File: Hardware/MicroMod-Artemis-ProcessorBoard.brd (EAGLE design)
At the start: 22 x 22 mm, 40 parts, among them J1 MICROMOD-2222, U1 ARTEMIS_MODULESMD, U2 TSV524, U6 CH340E_MSOP10, Y1 32.768kHz

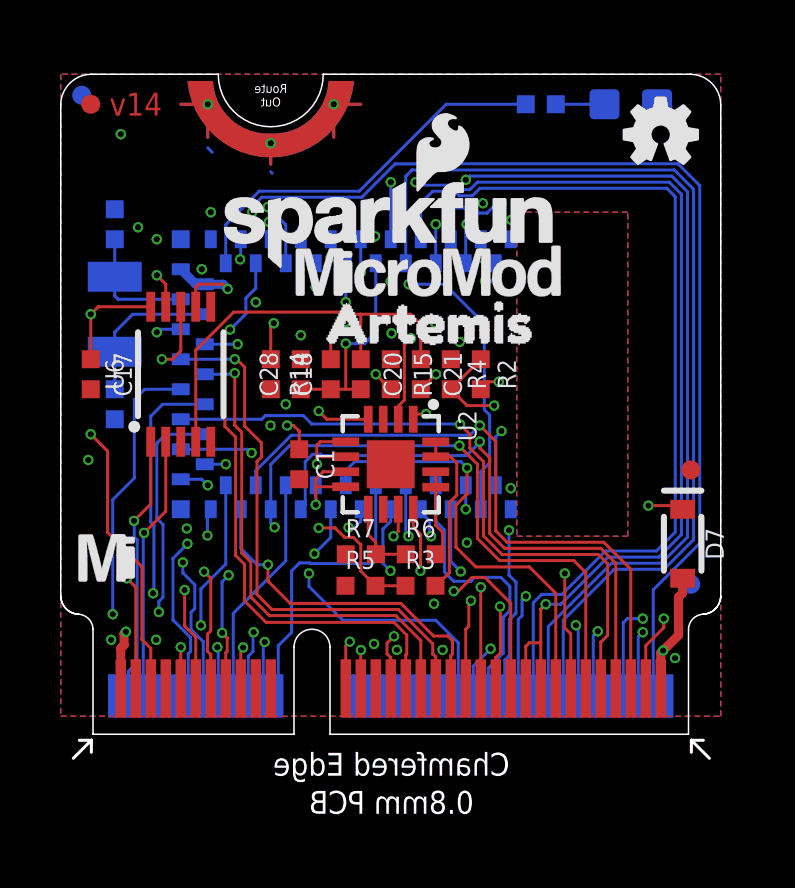
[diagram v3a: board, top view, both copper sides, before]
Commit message: Connect SPI pins to support Quad SPI. Move TX1 to AD12
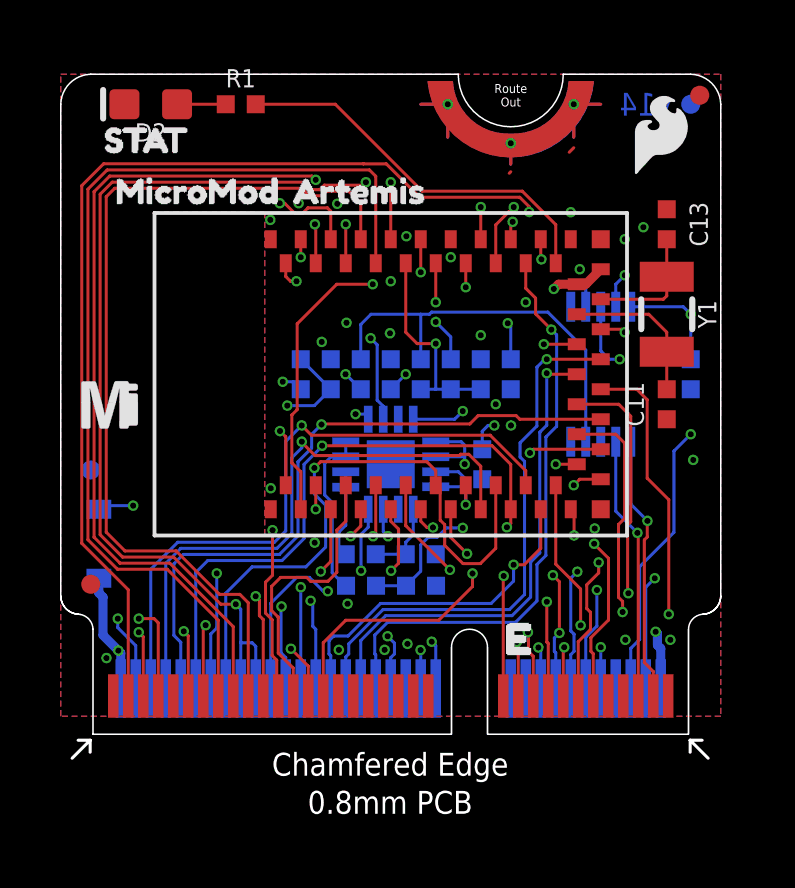
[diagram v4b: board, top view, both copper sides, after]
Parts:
- moved FRAME1 39.8 mm to (-8.89, -8.89), flipped to the top
- moved LOGO4 27.1 mm to (24.5, 50.8), flipped to the top
- moved FD2 20.6 mm to (21.3, 21.3), flipped to the top
- moved U$4 20.6 mm to (0.70, 19.8), flipped to the top
- moved C17 20.0 mm to (21.0, 12.0), flipped to the bottom
- moved FD1 20.0 mm to (1.00, 5.00), flipped to the top
- moved FD3 20.0 mm to (21.0, 21.0), flipped to the bottom
- moved FD4 20.0 mm to (1.00, 8.81), flipped to the bottom
- moved U$3 19.8 mm to (1.10, 18.1), flipped to the top
- moved D7 19.5 mm to (1.27, 6.35), flipped to the bottom
- moved U$7 19.0 mm to (20.5, 5.90), flipped to the bottom
- moved U$1 18.8 mm to (1.60, 11.0), flipped to the top
- moved C11 18.4 mm to (20.2, 11.0), flipped to the top
- moved C13 18.4 mm to (20.2, 17.0), flipped to the top
- moved Y1 18.4 mm to (20.2, 14.0), flipped to the top
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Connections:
- net SDIO_DATA1 renamed QSPI1
- net SDIO_DATA2 renamed QSPI2
- net SPI_!CS! renamed SPI_!CS!/QSPI3
- net SPI_MISO renamed SPI_MISO/QSPI0
- net SPI_MOSI renamed SPI_MOSI/QSPI_!CS!
- removed net ADC_D-: J1.65, U1.~AD12
- removed net SPI_SCK: J1.60, U1.~D5
- removed net TX1: J1.17, U1.~D24
- new net SPI_SCK/QSPI_CLK: J1.60, U1.~D24, U1.~D5
- new net TX1/ADC_D-: J1.17, J1.65, U1.~AD12
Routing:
- net TX1/ADC_D-: track 0.00 -> 28.3 mm, vias 0 -> 3
- net ADC_D-: track 25.2 -> 0.00 mm, vias 2 -> 0
- net SPI_SCK/QSPI_CLK: track 0.00 -> 21.1 mm, vias 0 -> 1
- net SPI_SCK: track 14.7 -> 0.00 mm, vias 1 -> 0
- net TX1: track 7.75 -> 0.00 mm
- net SWDIO: track 9.82 -> 9.49 mm, vias 0 -> 2
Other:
- outline, holes or cut-outs redrawn

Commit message: Adding additional decoupling, change version to v16.
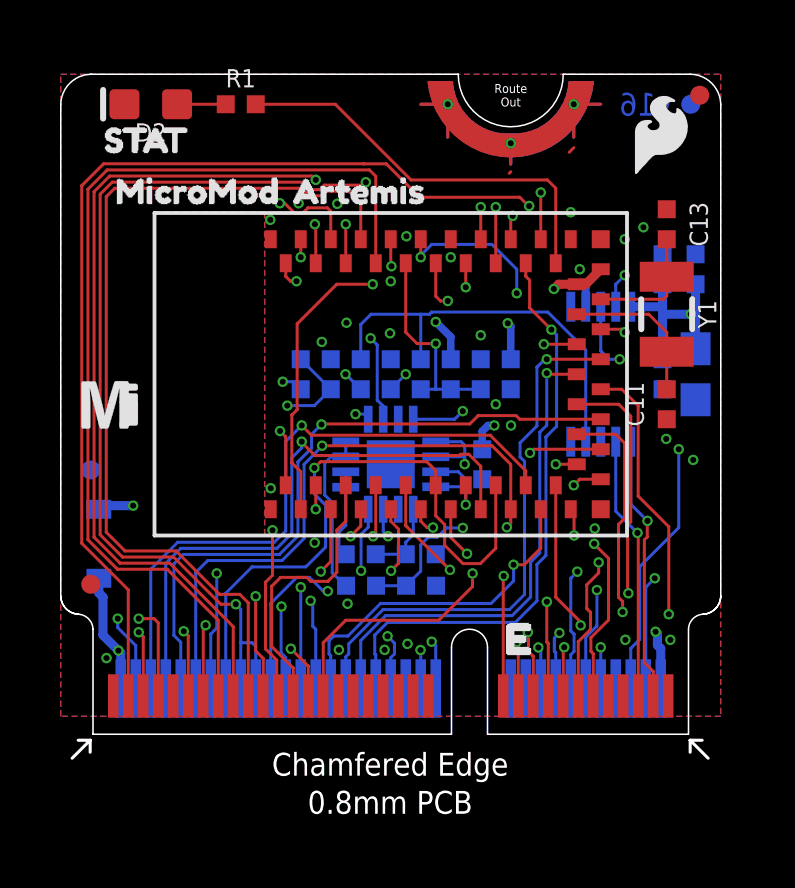
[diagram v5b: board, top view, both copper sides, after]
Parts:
- added C2: 0.22uF, SparkFun-Capacitors:0402-TIGHT
- added C3: 1.0uF, SparkFun-Capacitors:0402-TIGHT
- added C4: 10uF, SparkFun-Capacitors:0603
- R15: value 220KOHM-0402T-1/16W-1% -> 220K
- moved C17 3.62 mm to (20.1, 15.5), turned to 90 degrees
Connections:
- net SPI_SCK/QSPI_CLK renamed SPI_SCK/QSPI_SCK
- removed net CLKOUT: J1.56, J1.58, U1.D0
- new net CAM_MCLK: J1.56, J1.58, U1.~D18
- net 3.3V: now also C2.1, C3.1, C4.1
- net D0: now also U1.D0; no longer U1.D1
- net D1: now also U1.D1; no longer U1.D2
- net GND: now also C2.2, C3.2, C4.2
- net I2C_!INT!: now also U1.D2; no longer U1.~D18
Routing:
- net CAM_MCLK: track 0.00 -> 38.4 mm, vias 0 -> 3
- net CLKOUT: track 33.6 -> 0.00 mm, vias 3 -> 0
- net I2C_!INT!: track 15.5 -> 18.8 mm, vias 3 -> 2
- net 3.3V: track 17.7 -> 20.9 mm
- net GPIO5: track 41.7 -> 40.2 mm
- net D1: track 17.5 -> 18.8 mm
- net SCALED_BATT_VIN/3: track 19.8 -> 19.0 mm
- net D0: track 20.9 -> 21.7 mm
- net LED_BUILTIN: track 12.9 -> 13.7 mm
- net !RESET!: track 26.0 -> 25.5 mm
- net GND: vias 20 -> 21
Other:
- board text added: "v16"
- board text removed: "v14"

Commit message: Update SPI port 0/1 net names.
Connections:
- net SPI_!CS!/QSPI3 renamed SPI_!CS1!/QSPI3
- net SPI_!CS!1 renamed SPI_!CS!
- net SPI_MISO/QSPI0 renamed SPI_CIPO1/QSPI0
- net SPI_MISO1 renamed SPI_CIPO
- net SPI_MOSI/QSPI_!CS! renamed SPI_COPI1/QSPI_!CS!
- net SPI_MOSI1 renamed SPI_COPI
- net SPI_SCK/QSPI_SCK renamed SPI_SCK1/QSPI_SCK
- net SPI_SCK1 renamed SPI_SCK
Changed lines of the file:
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@@
 <elements>
 <element name="U1" library="SparkFun-IC-Microcontroller" package="ARTEMIS_FP" value="ARTEMIS_MODULESMD" x="11.5" y="12" smashed="yes" rot="R180">
-<attribute name="PROD_ID" value="SUB-14479" x="11.5" y="12" size="1.778" layer="27" font="vector" ratio="15" rot="R180" display="off"/>
+<attribute name="PROD_ID" value="SUB-14402" x="11.5" y="12" size="1.778" layer="27" font="vector" ratio="15" rot="R180" display="off"/>
 </element>
 <element name="FRAME1" library="SparkFun-Aesthetics" package="CREATIVE_COMMONS" value="FRAME-LEDGER" x="-8.89" y="-8.89" smashed="yes">
@@
 <wire x1="13.9352875" y1="11.1" x2="8.3009875" y2="11.1" width="0.1016" layer="2"/>
 </signal>
-<signal name="SPI_SCK1">
+<signal name="SPI_SCK">
 <contactref element="U1" pad="~D42"/>
 <wire x1="3.84568125" y1="6.1096" x2="2.143075" y2="6.1096" width="0.1016" layer="1"/>
@@
 <wire x1="5.292725" y1="4.66255625" x2="3.84568125" y2="6.1096" width="0.1016" layer="1"/>
 </signal>
-<signal name="SPI_MOSI1">
+<signal name="SPI_COPI">
 <contactref element="U1" pad="D38"/>
 <wire x1="5.75" y1="3.58736875" x2="3.63416875" y2="5.7032" width="0.1016" layer="1"/>
@@
 <wire x1="5.75" y1="1.275" x2="5.75" y2="3.58736875" width="0.1016" layer="1"/>
 </signal>
-<signal name="SPI_SCK/QSPI_SCK">
+<signal name="SPI_SCK1/QSPI_SCK">
 <contactref element="U1" pad="~D24"/>
 <contactref element="U1" pad="~D5"/>
@@
 <wire x1="8" y1="9.254875" x2="8.3626125" y2="9.6174875" width="0.1016" layer="15"/>
 </signal>
-<signal name="SPI_MISO/QSPI0">
+<signal name="SPI_CIPO1/QSPI0">
 <contactref element="U1" pad="~D22"/>
 <wire x1="15" y1="8.99391875" x2="15" y2="7.5" width="0.1016" layer="1"/>
@@
 <wire x1="8.1096" y1="6.52485" x2="8.1096" y2="8.99749375" width="0.1016" layer="16"/>
 </signal>
-<signal name="SPI_MOSI/QSPI_!CS!">
+<signal name="SPI_COPI1/QSPI_!CS!">
 <contactref element="U1" pad="D7"/>
 <wire x1="13" y1="7.5" x2="13" y2="6.5602" width="0.1016" layer="1"/>
@@
 <wire x1="5" y1="1.525" x2="5" y2="3.3416875" width="0.1016" layer="16"/>
 </signal>
-<signal name="SPI_!CS!/QSPI3">
+<signal name="SPI_!CS1!/QSPI3">
 <contactref element="U1" pad="~D23"/>
 <wire x1="3" y1="5.5" x2="3.9" y2="6.4" width="0.1016" layer="16"/>
@@
 <wire x1="17.41543125" y1="4.7446" x2="10.44478125" y2="4.7446" width="0.1016" layer="2"/>
 </signal>
-<signal name="SPI_MISO1">
+<signal name="SPI_CIPO">
 <contactref element="U1" pad="~D43"/>
 <wire x1="5.25" y1="3.8" x2="3.55" y2="5.5" width="0.1016" layer="1"/>
@@
 <wire x1="19.75" y1="1.275" x2="19.75" y2="2.094" width="0.1016" layer="1"/>
 </signal>
-<signal name="SPI_!CS!1">
+<signal name="SPI_!CS!">
 <contactref element="U1" pad="D41"/>
 <wire x1="14" y1="16.5" x2="14" y2="17.5714" width="0.1016" layer="1"/>

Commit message: Change 3.3V back feed diode to lower v-drop.
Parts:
- D7: value 1A/23V/620mV -> 3A/10V/280mV
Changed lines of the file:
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@@
 <?xml version="1.0" encoding="utf-8"?>
 <!DOCTYPE eagle SYSTEM "eagle.dtd">
-<eagle version="9.6.0">
+<eagle version="9.6.2">
 <drawing>
 <settings>
@@
 </element>
 <element name="LOGO1" library="SparkFun-Aesthetics" package="SFE_LOGO_NAME_FLAME_.1" value="SFE_LOGO_NAME_FLAME.1_INCH" x="11" y="17" smashed="yes" rot="MR0"/>
-<element name="D7" library="SparkFun-DiscreteSemi" package="SOD-323" value="1A/23V/620mV" x="1.27" y="6.35" smashed="yes" rot="MR270">
+<element name="D7" library="SparkFun-DiscreteSemi" package="SOD-323" value="3A/10V/280mV" x="1.27" y="6.35" smashed="yes" rot="MR270">
 <attribute name="NAME" x="0.508" y="6.35" size="0.6096" layer="26" font="vector" ratio="20" rot="MR270" align="bottom-center"/>
-<attribute name="PROD_ID" value="DIO-11623" x="1.27" y="7.62" size="1.778" layer="28" font="vector" ratio="15" rot="MR270" display="off"/>
-<attribute name="VALUE" x="2.032" y="6.35" size="0.6096" layer="28" font="vector" ratio="20" rot="MR270" align="top-center"/>
+<attribute name="PROD_ID" value="DIO-14072" x="1.27" y="7.62" size="1.778" layer="28" font="vector" ratio="15" rot="MR270" display="off"/>
+<attribute name="VALUE" value="3A/10V/280mV" x="2.032" y="6.35" size="0.6096" layer="28" font="vector" ratio="20" rot="MR270" align="top-center"/>
 </element>
 <element name="LOGO2" library="SparkFun-Aesthetics" package="SFE_LOGO_FLAME_.1" value="SFE_LOGO_FLAME.1_INCH" x="20" y="20" smashed="yes"/>

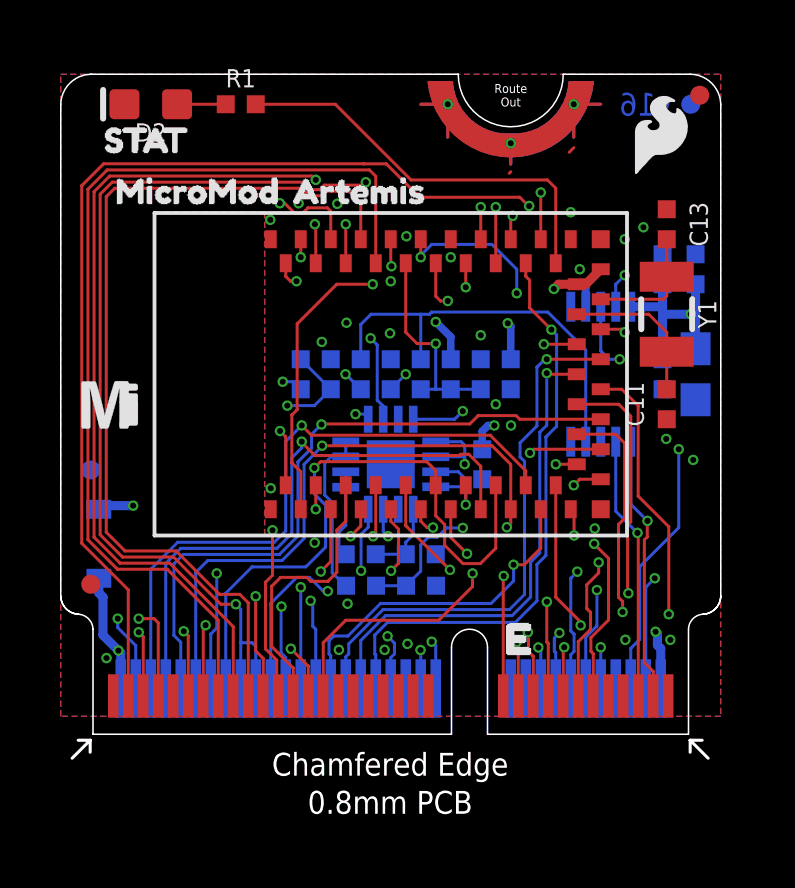
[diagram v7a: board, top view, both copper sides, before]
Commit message: Move CH340 to 3.3V side of diode. Replace D7 with 0.3uA leakage diode.
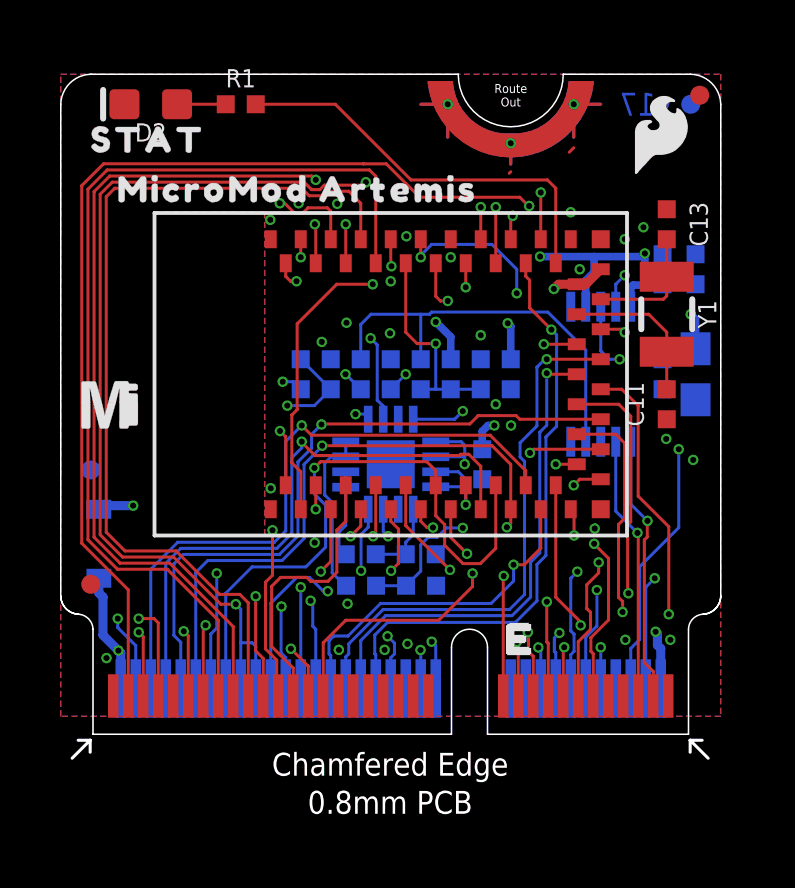
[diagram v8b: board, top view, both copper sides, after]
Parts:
- removed U$2: (no value), buzzard_labels:ARTEMIS0
- removed U$3: (no value), buzzard_labels:MICROMOD1
- removed U$4: (no value), SparkFun-Buzzard:STAT_TO_32
- removed U$6: (no value), buzzard_labels (1):ARTEMIS2
- added U$11: (no value), output:STAT0
- added U$8: (no value), output:MICROMOD_ARTEMIS0
- added U$9: (no value), output:ARTEMIS0
- D7: value 3A/10V/280mV -> 1A/23V/620mV
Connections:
- removed net 3.3V_MAIN: D7.A, J1.2, J1.74
- new net V_BATT: C1.1, C3.1, C4.1, D7.C, J1.72, R14.2, U1.VDD@36, U1.VDD@37, U2.2
- net 3.3V: now also D7.A, J1.2, J1.74; no longer C1.1, C3.1, C4.1, D7.C, J1.72, R14.2, U1.VDD@36, U1.VDD@37, U2.2
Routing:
- net 3.3V: track 20.9 -> 53.3 mm, vias 8 -> 5
- net 3.3V_MAIN: track 26.3 -> 0.00 mm, vias 2 -> 0
- net V_BATT: track 0.00 -> 18.4 mm, vias 0 -> 7
- added copper zone on layer 15, net V_BATT
- removed copper zone on layer 15, net 3.3V
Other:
- board text added: "v17"
- board text removed: "v16"
